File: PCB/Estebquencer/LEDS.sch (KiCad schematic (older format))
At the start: 44 parts

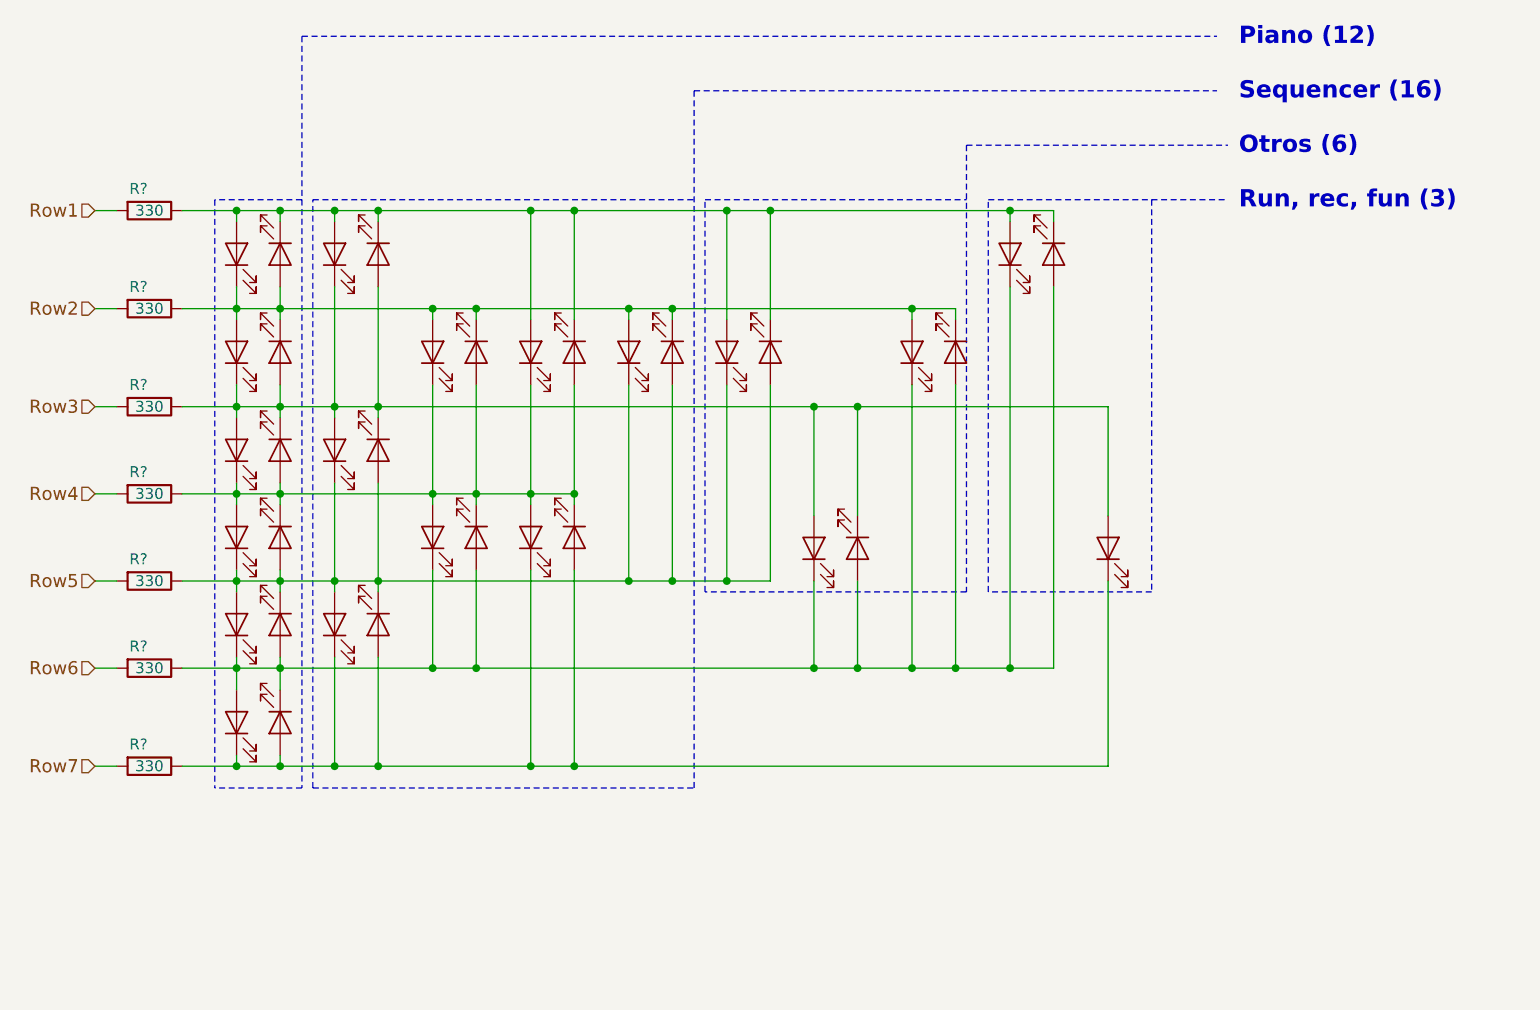
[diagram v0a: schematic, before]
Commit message: Se tuvo que cambiar el sistema de gestión de los LED y pulsadores. Con el charlieplexing no tenía los resultados esperados, así que se le añadió un HT16K33 para hacer las cosas más simples y fluídas. También se usará el mismo IC para la gestión de botones, ya que da opción.
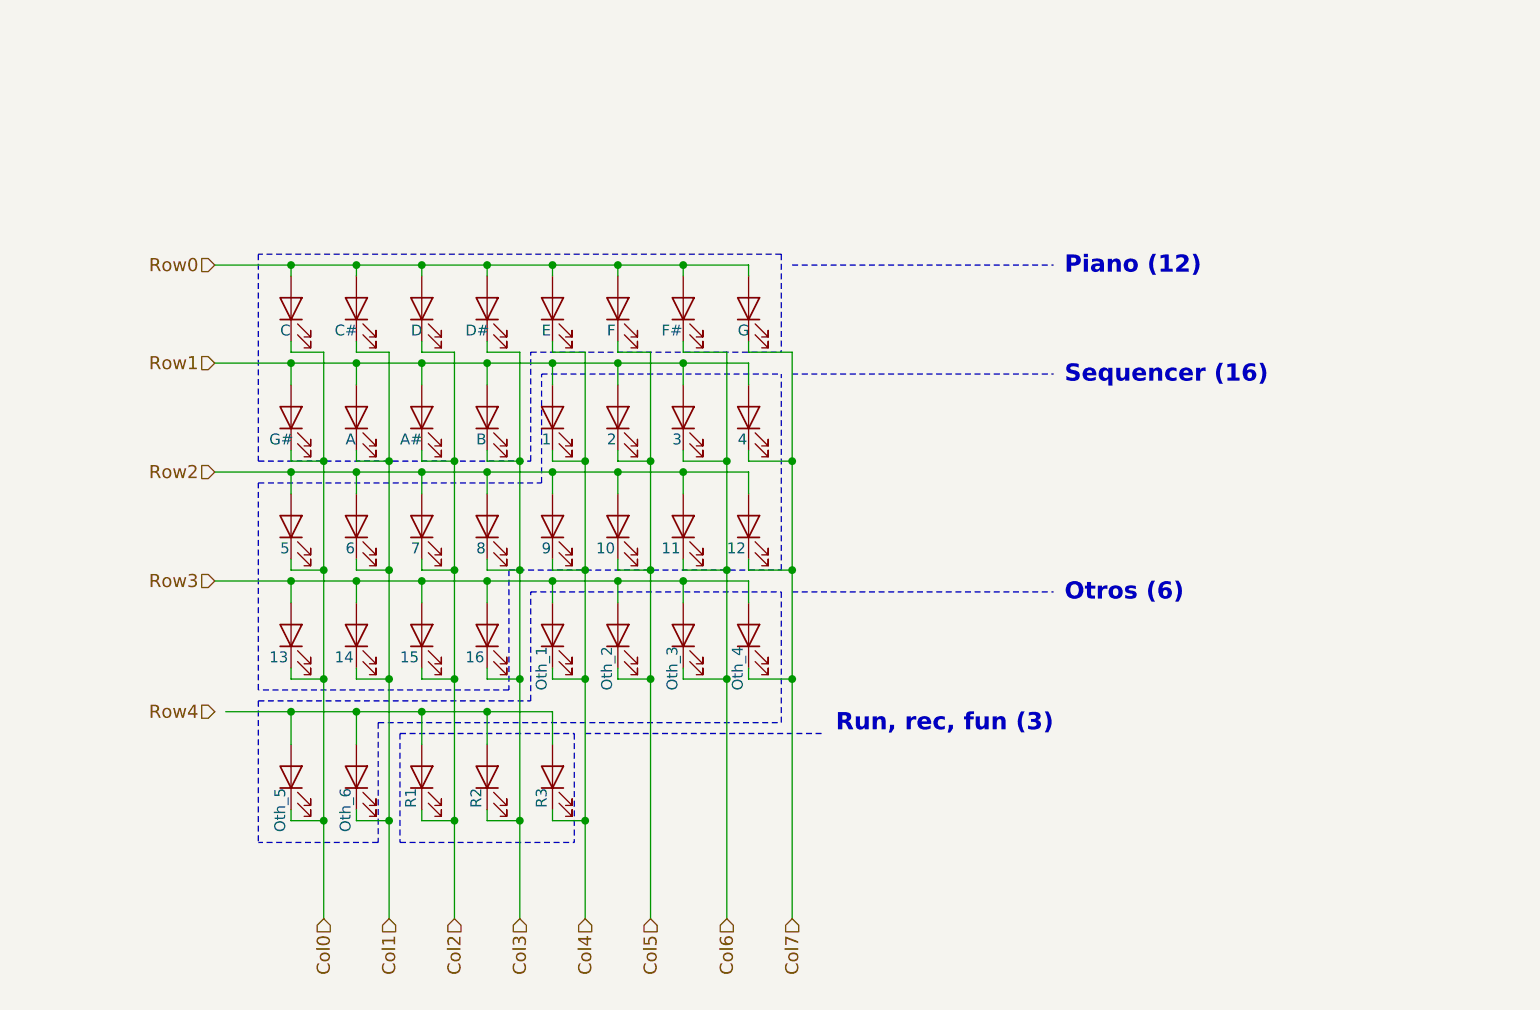
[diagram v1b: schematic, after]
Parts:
- removed D? (x37): L, symbol Device:LED
- removed R? (x7): 330, symbol Device:R
- added D?: A#, symbol Device:LED
- added D?: B, symbol Device:LED
- added D?: G#, symbol Device:LED
- added D?: A, symbol Device:LED
- added D?: 15, symbol Device:LED
- added D?: 16, symbol Device:LED
- added D?: F#, symbol Device:LED
- added D?: G, symbol Device:LED
- added D?: 13, symbol Device:LED
- added D?: 14, symbol Device:LED
- added D?: E, symbol Device:LED
- added D?: F, symbol Device:LED
- added D?: 7, symbol Device:LED
- added D?: 8, symbol Device:LED
- added D?: 11, symbol Device:LED
- added D?: 12, symbol Device:LED
- added D?: 1, symbol Device:LED
- added D?: 2, symbol Device:LED
- added D?: Oth_1, symbol Device:LED
- added D?: Oth_2, symbol Device:LED
- added D?: D, symbol Device:LED
- added D?: D#, symbol Device:LED
- added D?: 9, symbol Device:LED
- added D?: 10, symbol Device:LED
- added D?: Oth_3, symbol Device:LED
- added D?: Oth_4, symbol Device:LED
- added D?: Oth_5, symbol Device:LED
- added D?: Oth_6, symbol Device:LED
- added D?: R1, symbol Device:LED
- added D?: R2, symbol Device:LED
- added D?: C, symbol Device:LED
- added D?: C#, symbol Device:LED
- added D?: 5, symbol Device:LED
- added D?: 6, symbol Device:LED
- added D?: 3, symbol Device:LED
- added D?: 4, symbol Device:LED
- added D?: R3, symbol Device:LED
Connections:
- net Row1: now also D?.2 (A), D?.2 (A), D?.2 (A), D?.2 (A), D?.2 (A), D?.2 (A), D?.2 (A), D?.2 (A)
- net Row2: now also D?.2 (A), D?.2 (A), D?.2 (A), D?.2 (A), D?.2 (A), D?.2 (A), D?.2 (A), D?.2 (A)
- net Row3: now also D?.2 (A), D?.2 (A), D?.2 (A), D?.2 (A), D?.2 (A), D?.2 (A), D?.2 (A), D?.2 (A)
- new net: D?.2 (A), D?.2 (A), D?.2 (A), D?.2 (A), D?.2 (A)
- new net Col0: D?.1 (K), D?.1 (K), D?.1 (K), D?.1 (K), D?.1 (K)
- new net Col1: D?.1 (K), D?.1 (K), D?.1 (K), D?.1 (K), D?.1 (K)
- new net Col2: D?.1 (K), D?.1 (K), D?.1 (K), D?.1 (K), D?.1 (K)
- new net Col3: D?.1 (K), D?.1 (K), D?.1 (K), D?.1 (K), D?.1 (K)
- new net Col4: D?.1 (K), D?.1 (K), D?.1 (K), D?.1 (K), D?.1 (K)
- new net Col5: D?.1 (K), D?.1 (K), D?.1 (K), D?.1 (K)
- new net Col6: D?.1 (K), D?.1 (K), D?.1 (K), D?.1 (K)
- new net Col7: D?.1 (K), D?.1 (K), D?.1 (K), D?.1 (K)
- new net Row0: D?.2 (A), D?.2 (A), D?.2 (A), D?.2 (A), D?.2 (A), D?.2 (A), D?.2 (A), D?.2 (A)

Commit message: Había un pin desconectador de la matriz de LEDs
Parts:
- gave numbers to parts that had none: 37
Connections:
- net Row4: now also D10.2 (A), D15.2 (A), D20.2 (A), D25.2 (A), D5.2 (A)
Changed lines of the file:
@@
 Row0
 $Comp
-L Device:LED D?
+L Device:LED D12
 U 1 1 5E438969
 P 5300 3100
-F 0 "D?" V 5338 2983 50  0001 R CNN
+F 0 "D12" V 5338 2983 50  0001 R CNN
 F 1 "A#" V 5200 3200 50  0000 R CNN
 F 2 "" H 5300 3100 50  0001 C CNN
@@
 $EndComp
 $Comp
-L Device:LED D?
+L Device:LED D17
 U 1 1 5E43896F
 P 5600 3100
-F 0 "D?" V 5638 2983 50  0001 R CNN
+F 0 "D17" V 5638 2983 50  0001 R CNN
 F 1 "B" V 5500 3150 50  0000 R CNN
 F 2 "" H 5600 3100 50  0001 C CNN
@@
 $EndComp
 $Comp
-L Device:LED D?
+L Device:LED D2
 U 1 1 5E43897B
 P 4700 3100
-F 0 "D?" V 4738 2983 50  0001 R CNN
+F 0 "D2" V 4738 2983 50  0001 R CNN
 F 1 "G#" V 4600 3200 50  0000 R CNN
 F 2 "" H 4700 3100 50  0001 C CNN
@@
 $EndComp
 $Comp
-L Device:LED D?
+L Device:LED D7
 U 1 1 5E438981
 P 5000 3100
-F 0 "D?" V 5038 2983 50  0001 R CNN
+F 0 "D7" V 5038 2983 50  0001 R CNN
 F 1 "A" V 4900 3150 50  0000 R CNN
 F 2 "" H 5000 3100 50  0001 C CNN
@@
 $EndComp
 $Comp
-L Device:LED D?
+L Device:LED D14
 U 1 1 5E43898B
 P 5300 4100
-F 0 "D?" V 5338 3983 50  0001 R CNN
+F 0 "D14" V 5338 3983 50  0001 R CNN
 F 1 "15" V 5200 4200 50  0000 R CNN
 F 2 "" H 5300 4100 50  0001 C CNN
@@
 $EndComp
 $Comp
-L Device:LED D?
+L Device:LED D19
 U 1 1 5E438991
 P 5600 4100
-F 0 "D?" V 5638 3983 50  0001 R CNN
+F 0 "D19" V 5638 3983 50  0001 R CNN
 F 1 "16" V 5500 4200 50  0000 R CNN
 F 2 "" H 5600 4100 50  0001 C CNN
@@
 $EndComp
 $Comp
-L Device:LED D?
+L Device:LED D30
 U 1 1 5E438997
 P 6500 2600
-F 0 "D?" V 6538 2483 50  0001 R CNN
+F 0 "D30" V 6538 2483 50  0001 R CNN
 F 1 "F#" V 6400 2700 50  0000 R CNN
 F 2 "" H 6500 2600 50  0001 C CNN
@@
 $EndComp
 $Comp
-L Device:LED D?
+L Device:LED D34
 U 1 1 5E43899D
 P 6800 2600
-F 0 "D?" V 6838 2483 50  0001 R CNN
+F 0 "D34" V 6838 2483 50  0001 R CNN
 F 1 "G" V 6700 2650 50  0000 R CNN
 F 2 "" H 6800 2600 50  0001 C CNN
@@
 $EndComp
 $Comp
-L Device:LED D?
+L Device:LED D4
 U 1 1 5E4389A7
 P 4700 4100
-F 0 "D?" V 4738 3983 50  0001 R CNN
+F 0 "D4" V 4738 3983 50  0001 R CNN
 F 1 "13" V 4600 4200 50  0000 R CNN
 F 2 "" H 4700 4100 50  0001 C CNN
@@
 $EndComp
 $Comp
-L Device:LED D?
+L Device:LED D9
 U 1 1 5E4389AD
 P 5000 4100
-F 0 "D?" V 5038 3983 50  0001 R CNN
+F 0 "D9" V 5038 3983 50  0001 R CNN
 F 1 "14" V 4900 4200 50  0000 R CNN
 F 2 "" H 5000 4100 50  0001 C CNN
@@
 $EndComp
 $Comp
-L Device:LED D?
+L Device:LED D21
 U 1 1 5E4389B3
 P 5900 2600
-F 0 "D?" V 5938 2483 50  0001 R CNN
+F 0 "D21" V 5938 2483 50  0001 R CNN
 F 1 "E" V 5800 2650 50  0000 R CNN
 F 2 "" H 5900 2600 50  0001 C CNN
@@
 $EndComp
 $Comp
-L Device:LED D?
+L Device:LED D26
 U 1 1 5E4389B9
 P 6200 2600
-F 0 "D?" V 6238 2483 50  0001 R CNN
+F 0 "D26" V 6238 2483 50  0001 R CNN
 F 1 "F" V 6100 2650 50  0000 R CNN
 F 2 "" H 6200 2600 50  0001 C CNN
@@
 $EndComp
 $Comp
-L Device:LED D?
+L Device:LED D13
 U 1 1 5E4389C3
 P 5300 3600
-F 0 "D?" V 5338 3483 50  0001 R CNN
+F 0 "D13" V 5338 3483 50  0001 R CNN
 F 1 "7" V 5200 3650 50  0000 R CNN
 F 2 "" H 5300 3600 50  0001 C CNN
@@
 $EndComp
 $Comp
-L Device:LED D?
+L Device:LED D18
 U 1 1 5E4389C9
 P 5600 3600
-F 0 "D?" V 5638 3483 50  0001 R CNN
+F 0 "D18" V 5638 3483 50  0001 R CNN
 F 1 "8" V 5500 3650 50  0000 R CNN
 F 2 "" H 5600 3600 50  0001 C CNN
@@
 $EndComp
 $Comp
-L Device:LED D?
+L Device:LED D32
 U 1 1 5E4389CF
 P 6500 3600
-F 0 "D?" V 6538 3483 50  0001 R CNN
+F 0 "D32" V 6538 3483 50  0001 R CNN
 F 1 "11" V 6400 3700 50  0000 R CNN
 F 2 "" H 6500 3600 50  0001 C CNN
@@
 $EndComp
 $Comp
-L Device:LED D?
+L Device:LED D36
 U 1 1 5E4389D5
 P 6800 3600
-F 0 "D?" V 6838 3483 50  0001 R CNN
+F 0 "D36" V 6838 3483 50  0001 R CNN
 F 1 "12" V 6700 3700 50  0000 R CNN
 F 2 "" H 6800 3600 50  0001 C CNN
@@
 $EndComp
 $Comp
-L Device:LED D?
+L Device:LED D22
 U 1 1 5E4389DB
 P 5900 3100
-F 0 "D?" V 5938 2983 50  0001 R CNN
+F 0 "D22" V 5938 2983 50  0001 R CNN
 F 1 "1" V 5800 3150 50  0000 R CNN
 F 2 "" H 5900 3100 50  0001 C CNN
@@
 $EndComp
 $Comp
-L Device:LED D?
+L Device:LED D27
 U 1 1 5E4389E1
 P 6200 3100
-F 0 "D?" V 6238 2983 50  0001 R CNN
+F 0 "D27" V 6238 2983 50  0001 R CNN
 F 1 "2" V 6100 3150 50  0000 R CNN
 F 2 "" H 6200 3100 50  0001 C CNN
@@
 $EndComp
 $Comp
-L Device:LED D?
+L Device:LED D24
 U 1 1 5E4389E7
 P 5900 4100
-F 0 "D?" V 5938 3983 50  0001 R CNN
+F 0 "D24" V 5938 3983 50  0001 R CNN
 F 1 "Oth_1" H 5850 4150 50  0000 R CNN
 F 2 "" H 5900 4100 50  0001 C CNN
@@
 $EndComp
 $Comp
-L Device:LED D?
+L Device:LED D29
 U 1 1 5E4389ED
 P 6200 4100
-F 0 "D?" V 6238 3983 50  0001 R CNN
+F 0 "D29" V 6238 3983 50  0001 R CNN
 F 1 "Oth_2" H 6150 4150 50  0000 R CNN
 F 2 "" H 6200 4100 50  0001 C CNN
@@
 $EndComp
 $Comp
-L Device:LED D?
+L Device:LED D11
 U 1 1 5E438A40
 P 5300 2600
-F 0 "D?" V 5338 2483 50  0001 R CNN
+F 0 "D11" V 5338 2483 50  0001 R CNN
 F 1 "D" V 5200 2650 50  0000 R CNN
 F 2 "" H 5300 2600 50  0001 C CNN
@@
 $EndComp
 $Comp
-L Device:LED D?
+L Device:LED D16
 U 1 1 5E438A46
 P 5600 2600
-F 0 "D?" V 5638 2483 50  0001 R CNN
+F 0 "D16" V 5638 2483 50  0001 R CNN
 F 1 "D#" V 5500 2700 50  0000 R CNN
 F 2 "" H 5600 2600 50  0001 C CNN
@@
 $EndComp
 $Comp
-L Device:LED D?
+L Device:LED D23
 U 1 1 5E438A52
 P 5900 3600
-F 0 "D?" V 5938 3483 50  0001 R CNN
+F 0 "D23" V 5938 3483 50  0001 R CNN
 F 1 "9" V 5800 3650 50  0000 R CNN
 F 2 "" H 5900 3600 50  0001 C CNN
@@
 $EndComp
 $Comp
-L Device:LED D?
+L Device:LED D28
 U 1 1 5E438A58
 P 6200 3600
-F 0 "D?" V 6238 3483 50  0001 R CNN
+F 0 "D28" V 6238 3483 50  0001 R CNN
 F 1 "10" V 6100 3700 50  0000 R CNN
 F 2 "" H 6200 3600 50  0001 C CNN
@@
 $EndComp
 $Comp
-L Device:LED D?
+L Device:LED D33
 U 1 1 5E438A64
 P 6500 4100
-F 0 "D?" V 6538 3983 50  0001 R CNN
+F 0 "D33" V 6538 3983 50  0001 R CNN
 F 1 "Oth_3" H 6450 4150 50  0000 R CNN
 F 2 "" H 6500 4100 50  0001 C CNN
@@
 $EndComp
 $Comp
-L Device:LED D?
+L Device:LED D37
 U 1 1 5E438A6A
 P 6800 4100
-F 0 "D?" V 6838 3983 50  0001 R CNN
+F 0 "D37" V 6838 3983 50  0001 R CNN
 F 1 "Oth_4" H 6750 4150 50  0000 R CNN
 F 2 "" H 6800 4100 50  0001 C CNN
@@
 $EndComp
 $Comp
-L Device:LED D?
+L Device:LED D5
 U 1 1 5E438A7A
 P 4700 4750
-F 0 "D?" V 4738 4633 50  0001 R CNN
+F 0 "D5" V 4738 4633 50  0001 R CNN
 F 1 "Oth_5" H 4650 4800 50  0000 R CNN
 F 2 "" H 4700 4750 50  0001 C CNN
@@
 $EndComp
 $Comp
-L Device:LED D?
+L Device:LED D10
 U 1 1 5E438A80
 P 5000 4750
-F 0 "D?" V 5038 4633 50  0001 R CNN
+F 0 "D10" V 5038 4633 50  0001 R CNN
 F 1 "Oth_6" H 4950 4800 50  0000 R CNN
 F 2 "" H 5000 4750 50  0001 C CNN
@@
 $EndComp
 $Comp
-L Device:LED D?
+L Device:LED D15
 U 1 1 5E438A9B
 P 5300 4750
-F 0 "D?" V 5338 4633 50  0001 R CNN
+F 0 "D15" V 5338 4633 50  0001 R CNN
 F 1 "R1" H 5250 4800 50  0000 R CNN
 F 2 "" H 5300 4750 50  0001 C CNN
@@
 $EndComp
 $Comp
-L Device:LED D?
+L Device:LED D20
 U 1 1 5E438AA1
 P 5600 4750
-F 0 "D?" V 5638 4633 50  0001 R CNN
+F 0 "D20" V 5638 4633 50  0001 R CNN
 F 1 "R2" H 5550 4800 50  0000 R CNN
 F 2 "" H 5600 4750 50  0001 C CNN
@@
 $EndComp
 $Comp
-L Device:LED D?
+L Device:LED D1
 U 1 1 5E438AB3
 P 4700 2600
-F 0 "D?" V 4738 2483 50  0001 R CNN
+F 0 "D1" V 4738 2483 50  0001 R CNN
 F 1 "C" V 4600 2650 50  0000 R CNN
 F 2 "" H 4700 2600 50  0001 C CNN
@@
 $EndComp
 $Comp
-L Device:LED D?
+L Device:LED D6
 U 1 1 5E438AB9
 P 5000 2600
-F 0 "D?" V 5038 2483 50  0001 R CNN
+F 0 "D6" V 5038 2483 50  0001 R CNN
 F 1 "C#" V 4900 2700 50  0000 R CNN
 F 2 "" H 5000 2600 50  0001 C CNN
@@
 $EndComp
 $Comp
-L Device:LED D?
+L Device:LED D3
 U 1 1 5E438AC6
 P 4700 3600
-F 0 "D?" V 4738 3483 50  0001 R CNN
+F 0 "D3" V 4738 3483 50  0001 R CNN
 F 1 "5" V 4600 3650 50  0000 R CNN
 F 2 "" H 4700 3600 50  0001 C CNN
@@
 $EndComp
 $Comp
-L Device:LED D?
+L Device:LED D8
 U 1 1 5E438ACC
 P 5000 3600
-F 0 "D?" V 5038 3483 50  0001 R CNN
+F 0 "D8" V 5038 3483 50  0001 R CNN
 F 1 "6" V 4900 3650 50  0000 R CNN
 F 2 "" H 5000 3600 50  0001 C CNN
@@
 $EndComp
 $Comp
-L Device:LED D?
+L Device:LED D31
 U 1 1 5E438ADA
 P 6500 3100
-F 0 "D?" V 6538 2983 50  0001 R CNN
+F 0 "D31" V 6538 2983 50  0001 R CNN
 F 1 "3" V 6400 3150 50  0000 R CNN
 F 2 "" H 6500 3100 50  0001 C CNN
@@
 $EndComp
 $Comp
-L Device:LED D?
+L Device:LED D35
 U 1 1 5E438AE0
 P 6800 3100
-F 0 "D?" V 6838 2983 50  0001 R CNN
+F 0 "D35" V 6838 2983 50  0001 R CNN
 F 1 "4" V 6700 3150 50  0000 R CNN
 F 2 "" H 6800 3100 50  0001 C CNN
@@
 $EndComp
 $Comp
-L Device:LED D?
+L Device:LED D25
 U 1 1 5E438AEF
 P 5900 4750
-F 0 "D?" V 5938 4633 50  0001 R CNN
+F 0 "D25" V 5938 4633 50  0001 R CNN
 F 1 "R3" H 5850 4800 50  0000 R CNN
 F 2 "" H 5900 4750 50  0001 C CNN
@@
 	5800 4400 5800 3900
 Wire Wire Line
-	4400 4450 4700 4450
-Wire Wire Line
 	5900 4450 5900 4600
 Connection ~ 5600 4450
@@
 Wire Wire Line
 	4850 4950 4850 5400
+Wire Wire Line
+	4350 4450 4700 4450
 $EndSCHEMATC
